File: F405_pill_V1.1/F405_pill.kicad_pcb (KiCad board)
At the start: 4 copper layers, 54.1 x 19.4 mm, 49 parts, among them J1 Conn_01x04_Male, J2 Conn_01x04_Male, J4 TYPE-C-31-M-12, U1 STM32F405RGTx, U2 TJA1050T/CM,118, U3 LM1117-3.3, U4 STM32F405_pill, U5 HT7550-1, Y1 Crystal_GND24

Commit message: minor part changes
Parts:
- C16: footprint Capacitor_Tantalum_SMD:CP_EIA-3216-18_Kemet-A -> Capacitor_SMD:C_0603_1608Metric
- R3, R4: value 60 ohm -> 100Ω; footprint Resistor_SMD:R_0603_1608Metric -> Resistor_SMD:R_0402_1005Metric
- U2: footprint Package_TO_SOT_SMD:SOT-23-8 -> Package_SO:SOIC-8_3.9x4.9mm_P1.27mm
- U5: value HT7550-1 -> HT7550
- moved C16 11.1 mm to (134.3, 81.2), turned to 90 degrees
- moved C22 11.0 mm to (142.3, 88.3), turned to -90 degrees
- moved C15 2.41 mm to (143.4, 83.4), turned to 90 degrees
- moved C14 1.81 mm to (143.4, 79.5)
- moved C13 1.73 mm to (143.4, 81.5)
- moved R4 1.48 mm to (144.4, 83.3)
- moved R3 1.03 mm to (144.4, 80.4), turned to 90 degrees
- moved U5 0.50 mm to (131.0, 81.2), turned to 90 degrees
- moved U2 0.30 mm to (138.8, 81.2)
- moved U3 0.13 mm to (136.2, 87.6)
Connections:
- C16 pad 1: +3V3 -> VDO_I
- C22 pad 1: VDO_I -> +3V3
- U5 pad 1: VDO_I -> GND
- U5 pad 2: GND -> +5V
- U5 pad 3: +5V -> VDO_I
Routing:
- net +5V: track 100.5 -> 94.6 mm, vias 3 -> 4
- net GND: track 75.7 -> 69.9 mm, vias 94 -> 89
- net Net-(C14-Pad1): track 10.6 -> 8.11 mm, vias 2 -> 0
- net PB8: track 28.1 -> 26.2 mm
- net Net-(C15-Pad1): track 9.14 -> 7.52 mm
- net PB3: track 15.0 -> 13.5 mm
- net PC6: track 42.0 -> 43.3 mm
- net PB15: track 14.0 -> 12.7 mm
- net VDO_I: track 5.46 -> 4.30 mm
- net PB9: track 28.8 -> 27.8 mm
- net Net-(C6-Pad1): track 7.43 -> 6.51 mm
- net Net-(C13-Pad1): track 3.78 -> 2.91 mm
- net +3V3: track 30.2 -> 29.9 mm, vias 10 -> 12

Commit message: minor part changes
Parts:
- moved D1 28.5 mm to (130.5, 85.9), turned to 90 degrees
- moved D3 28.5 mm to (102.9, 78.8), turned to 0 degrees
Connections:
- D1 pad 2: PC9 -> +3V3
- D3 pad 2: +3V3 -> PC9
- R7 pad 2: Net-(D1-Pad1) -> Net-(D3-Pad1)
- R9 pad 2: Net-(D3-Pad1) -> Net-(D1-Pad1)
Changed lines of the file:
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@@
       (net 2 "GND") (pintype "passive"))
     (pad "2" smd roundrect (at 0.51 0 90) (size 0.54 0.64) (layers "F.Cu" "F.Paste" "F.Mask") (roundrect_rratio 0.25)
-      (net 60 "Net-(D3-Pad1)") (pintype "passive"))
+      (net 55 "Net-(D1-Pad1)") (pintype "passive"))
     (model "${KICAD6_3DMODEL_DIR}/Resistor_SMD.3dshapes/R_0402_1005Metric.wrl"
       (offset (xyz 0 0 0))
@@
   )
   (footprint "LED_SMD:LED_0603_1608Metric" (layer "F.Cu")
-    (at 130.5 85.9 90)
+    (at 102.9 78.8)
     (descr "LED SMD 0603 (1608 Metric), square (rectangular) end terminal, IPC_7351 nominal, (Body size source: http://www.tortai-tech.com/upload/download/2011102023233369053.pdf), generated with kicad-footprint-generator")
     (tags "LED")
@@
     (property "Sheetname" "")
     (attr smd)
-    (fp_text reference "D3" (at 0 -1.43 90) (layer "F.SilkS") hide
+    (fp_text reference "D3" (at 0 -1.43) (layer "F.SilkS") hide
       (effects (font (size 1 1) (thickness 0.15)))
     )
-    (fp_text value "RED" (at 0 1.43 90) (layer "F.Fab")
+    (fp_text value "RED" (at 0 1.43) (layer "F.Fab")
       (effects (font (size 1 1) (thickness 0.15)))
     )
-    (fp_text user "${REFERENCE}" (at 0 0 90) (layer "F.Fab")
+    (fp_text user "${REFERENCE}" (at 0 0) (layer "F.Fab")
       (effects (font (size 0.4 0.4) (thickness 0.06)))
     )
@@
     (fp_line (start 0.8 0.4) (end 0.8 -0.4) (layer "F.Fab") (width 0.1))
     (fp_line (start -0.5 -0.4) (end -0.8 -0.1) (layer "F.Fab") (width 0.1))
-    (pad "1" smd roundrect (at -0.7875 0 90) (size 0.875 0.95) (layers "F.Cu" "F.Paste" "F.Mask") (roundrect_rratio 0.25)
+    (pad "1" smd roundrect (at -0.7875 0) (size 0.875 0.95) (layers "F.Cu" "F.Paste" "F.Mask") (roundrect_rratio 0.25)
       (net 60 "Net-(D3-Pad1)") (pinfunction "K") (pintype "passive"))
-    (pad "2" smd roundrect (at 0.7875 0 90) (size 0.875 0.95) (layers "F.Cu" "F.Paste" "F.Mask") (roundrect_rratio 0.25)
-      (net 4 "+3V3") (pinfunction "A") (pintype "passive"))
+    (pad "2" smd roundrect (at 0.7875 0) (size 0.875 0.95) (layers "F.Cu" "F.Paste" "F.Mask") (roundrect_rratio 0.25)
+      (net 42 "PC9") (pinfunction "A") (pintype "passive"))
     (model "${KICAD6_3DMODEL_DIR}/LED_SMD.3dshapes/LED_0603_1608Metric.wrl"
       (offset (xyz 0 0 0))
@@
   )
   (footprint "LED_SMD:LED_0603_1608Metric" (layer "F.Cu")
-    (at 102.9 78.8)
+    (at 130.5 85.9 90)
     (descr "LED SMD 0603 (1608 Metric), square (rectangular) end terminal, IPC_7351 nominal, (Body size source: http://www.tortai-tech.com/upload/download/2011102023233369053.pdf), generated with kicad-footprint-generator")
     (tags "LED")
@@
     (property "Sheetname" "")
     (attr smd)
-    (fp_text reference "D1" (at 0 -1.43) (layer "F.SilkS") hide
+    (fp_text reference "D1" (at 0 -1.43 90) (layer "F.SilkS") hide
       (effects (font (size 1 1) (thickness 0.15)))
     )
-    (fp_text value "BLU" (at 0 1.43) (layer "F.Fab")
+    (fp_text value "BLU" (at 0 1.43 90) (layer "F.Fab")
       (effects (font (size 1 1) (thickness 0.15)))
     )
-    (fp_text user "${REFERENCE}" (at 0 0) (layer "F.Fab")
+    (fp_text user "${REFERENCE}" (at 0 0 90) (layer "F.Fab")
       (effects (font (size 0.4 0.4) (thickness 0.06)))
     )
@@
     (fp_line (start -0.5 -0.4) (end -0.8 -0.1) (layer "F.Fab") (width 0.1))
     (fp_line (start -0.8 0.4) (end 0.8 0.4) (layer "F.Fab") (width 0.1))
-    (pad "1" smd roundrect (at -0.7875 0) (size 0.875 0.95) (layers "F.Cu" "F.Paste" "F.Mask") (roundrect_rratio 0.25)
+    (pad "1" smd roundrect (at -0.7875 0 90) (size 0.875 0.95) (layers "F.Cu" "F.Paste" "F.Mask") (roundrect_rratio 0.25)
       (net 55 "Net-(D1-Pad1)") (pinfunction "K") (pintype "passive"))
-    (pad "2" smd roundrect (at 0.7875 0) (size 0.875 0.95) (layers "F.Cu" "F.Paste" "F.Mask") (roundrect_rratio 0.25)
-      (net 42 "PC9") (pinfunction "A") (pintype "passive"))
+    (pad "2" smd roundrect (at 0.7875 0 90) (size 0.875 0.95) (layers "F.Cu" "F.Paste" "F.Mask") (roundrect_rratio 0.25)
+      (net 4 "+3V3") (pinfunction "A") (pintype "passive"))
     (model "${KICAD6_3DMODEL_DIR}/LED_SMD.3dshapes/LED_0603_1608Metric.wrl"
       (offset (xyz 0 0 0))
@@
       (net 2 "GND") (pintype "passive"))
     (pad "2" smd roundrect (at 0.51 0) (size 0.54 0.64) (layers "F.Cu" "F.Paste" "F.Mask") (roundrect_rratio 0.25)
-      (net 55 "Net-(D1-Pad1)") (pintype "passive"))
+      (net 60 "Net-(D3-Pad1)") (pintype "passive"))
     (model "${KICAD6_3DMODEL_DIR}/Resistor_SMD.3dshapes/R_0402_1005Metric.wrl"
       (offset (xyz 0 0 0))
@@
   (segment (start 122.635107 85.072) (end 120.617106 87.09) (width 0.16) (layer "B.Cu") (net 54))
   (segment (start 128.718 85.072) (end 122.635107 85.072) (width 0.16) (layer "B.Cu") (net 54))
-  (segment (start 102.1125 78.8) (end 100.86 78.8) (width 0.16) (layer "F.Cu") (net 55))
-  (segment (start 100.86 78.8) (end 100.7 78.64) (width 0.16) (layer "F.Cu") (net 55))
+  (segment (start 130.9 87.946) (end 130.9 87.0875) (width 0.16) (layer "F.Cu") (net 55))
+  (segment (start 130.9 87.0875) (end 130.5 86.6875) (width 0.16) (layer "F.Cu") (net 55))
   (segment (start 130 78.09) (end 135.954 78.09) (width 0.16) (layer "F.Cu") (net 56))
   (segment (start 118.167 85.429) (end 119.281 85.429) (width 0.16) (layer "F.Cu") (net 56))
@@
   (segment (start 144.62 83.77) (end 145.5 84.65) (width 0.16) (layer "F.Cu") (net 59))
   (segment (start 145.95 84.65) (end 146.982 85.682) (width 0.16) (layer "F.Cu") (net 59))
-  (segment (start 130.9 87.946) (end 130.9 87.0875) (width 0.16) (layer "F.Cu") (net 60))
-  (segment (start 130.9 87.0875) (end 130.5 86.6875) (width 0.16) (layer "F.Cu") (net 60))
+  (segment (start 102.1125 78.8) (end 100.86 78.8) (width 0.16) (layer "F.Cu") (net 60))
+  (segment (start 100.86 78.8) (end 100.7 78.64) (width 0.16) (layer "F.Cu") (net 60))
   (segment (start 97.16 76.735) (end 97 76.735) (width 0.16) (layer "F.Cu") (net 61))
   (segment (start 97.625 82.135) (end 97.625 77.2) (width 0.16) (layer "F.Cu") (net 61))

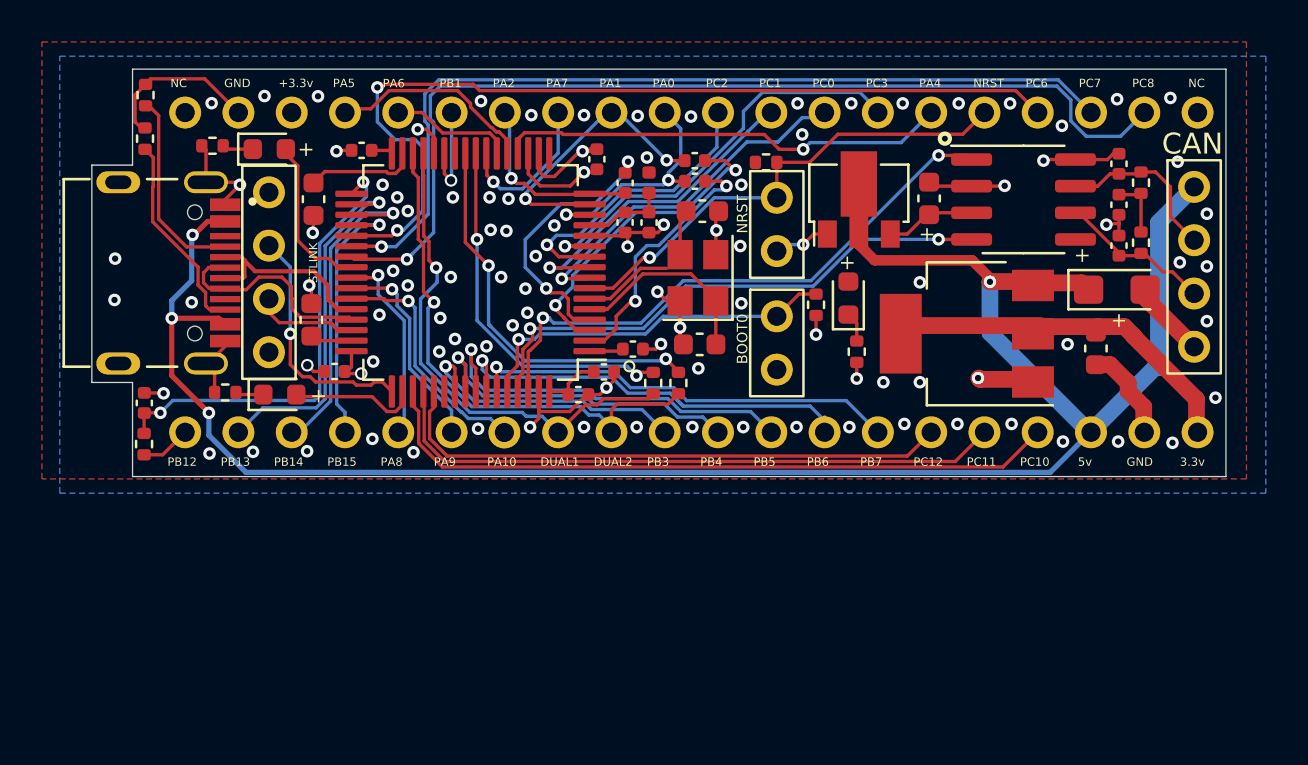
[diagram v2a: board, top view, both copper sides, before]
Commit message: fixed 2 footprints, fiddled with some vias
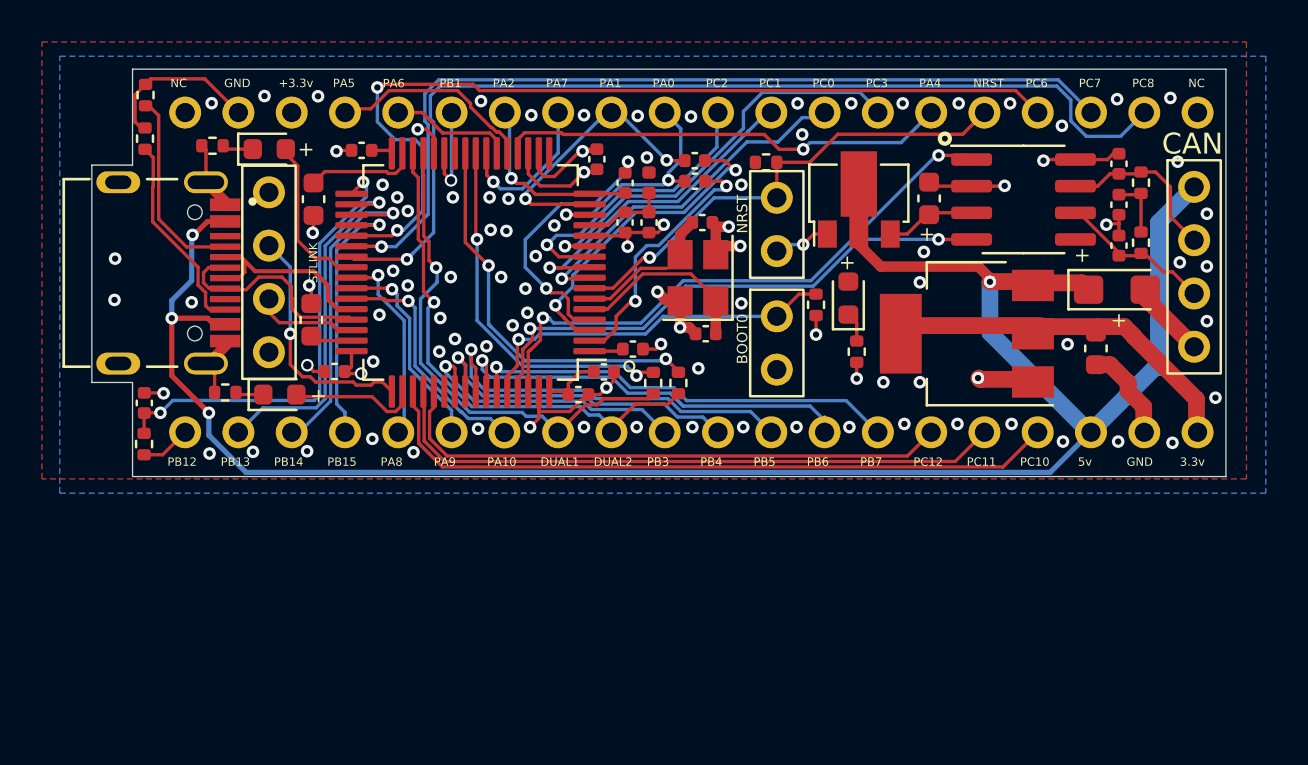
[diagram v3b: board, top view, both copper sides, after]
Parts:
- C3, C6: footprint Capacitor_SMD:C_0603_1608Metric -> Capacitor_SMD:C_0402_1005Metric
- moved C3 0.58 mm to (123.7, 87.6)
- moved C6 0.54 mm to (123.5, 82.3)
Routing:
- net GND: track 69.9 -> 69.1 mm
- net Net-(C3-Pad1): track 9.38 -> 8.67 mm
- net DUAL2: track 25.4 -> 24.8 mm

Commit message: manually merge F405_pill_V1.1
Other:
- board text added: "Manually set these parts to these orientations U1 90 U2 270 U3 0 U5 270 Updated U5 to lcsc# C6186"
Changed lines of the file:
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@@
     (effects (font (size 0.4 0.4) (thickness 0.06)))
+  )
+  (gr_text "Manually set these parts to these orientations\nU1 90\nU2 270\nU3 0\nU5 270\nUpdated U5 to lcsc# C6186" (at 93.35 101.05) (layer "F.SilkS")
+    (effects (font (size 1 1) (thickness 0.15)) (justify left))
   )
   (gr_text "PC0" (at 129.316 75.66) (layer "F.SilkS")
